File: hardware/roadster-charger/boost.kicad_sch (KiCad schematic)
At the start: 25 parts, among them Q1 CSD19532Q5B, U4 LTC3786EUD#TRPBF, U5 DAC70501MDQFR

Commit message: fix accidental schem. grid change, add footprints and MPNs
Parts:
- C12: footprint (none) -> Capacitor_SMD:C_0603_1608Metric; MPN (none) -> C0603C153K4REC7867
- C13: footprint (none) -> Capacitor_SMD:C_0603_1608Metric; MPN (none) -> C0603C221K1RAC7867
- C14: footprint (none) -> Capacitor_SMD:C_0805_2012Metric; MPN (none) -> CC0805KRX7R9BB104
- C15: footprint (none) -> Capacitor_SMD:C_0603_1608Metric; MPN (none) -> C1608X5R1E475K080AC
- C21, C22: footprint (none) -> Capacitor_SMD:C_0603_1608Metric; MPN (none) -> CL10B104KB8NNNC
- D5: MPN (none) -> BAS170WS-E3-08
- Q1: MPN (none) -> CSD19532Q5B
- R10: footprint (none) -> Resistor_SMD:R_0603_1608Metric; MPN (none) -> RC0603FR-07475KL
- R11: footprint (none) -> Resistor_SMD:R_0603_1608Metric; MPN (none) -> RC0603FR-1312K1L
- R12: footprint (none) -> Resistor_SMD:R_1206_3216Metric; MPN (none) -> WSLP12068L000FEA
- R13, R9: footprint (none) -> Resistor_SMD:R_0603_1608Metric; MPN (none) -> RC0603FR-078K66L
- U4: footprint QFN-16_UD -> LTC3786EUD_TRPBF:QFN-16_UD; Availability In Stock -> (none); Check_prices https://www.snapeda.com/parts/LTC3786EUD%23TRPBF/Analog+Dev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 -> (none); MANUFACTURER_PART_NUMBER ltc3786eud#pbf -> (none); MF Analog Devices -> (none); MP LTC3786EUD#TRPBF -> (none); MPN (none) -> LTC3786EUD#TRPBF; Purchase-URL https://pricing.snapeda.com/search?q=LTC3786EUD#TRPBF&ref=e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 -> (none); SnapEDA_Link https://www.snapeda.com/parts/LTC3786EUD%23TRPBF/Analog+Dev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 -> (none); VENDOR LinearTech -> (none)
- U5: footprint WSON8_2P1X2P1_TEX -> DAC70501:WSON8_2P1X2P1_TEX; MPN (none) -> DAC70501MDQFR
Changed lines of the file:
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@@
       (effects (font (size 1.524 1.524)))
     )
-    (property "Footprint" "WSON8_2P1X2P1_TEX" (at 134.62 107.95 0)
+    (property "Footprint" "DAC70501:WSON8_2P1X2P1_TEX" (at 134.62 107.95 0)
       (effects (font (size 1.27 1.27) italic) hide)
     )
     (property "Datasheet" "DAC70501MDQFR" (at 134.62 107.95 0)
       (effects (font (size 1.27 1.27) italic) hide)
+    )
+    (property "MPN" "DAC70501MDQFR" (at 134.62 111.76 0)
+      (effects (font (size 1.27 1.27)) hide)
     )
     (pin "1")
@@
       (effects (font (size 1.27 1.27)) (justify right))
     )
-    (property "Footprint" "" (at 191.77 146.05 0)
+    (property "Footprint" "Capacitor_SMD:C_0603_1608Metric" (at 191.77 146.05 0)
       (effects (font (size 1.27 1.27)) hide)
     )
     (property "Datasheet" "~" (at 191.77 146.05 0)
+      (effects (font (size 1.27 1.27)) hide)
+    )
+    (property "MPN" "C0603C221K1RAC7867" (at 191.77 146.05 0)
       (effects (font (size 1.27 1.27)) hide)
     )
@@
       (effects (font (size 1.27 1.27)) (justify left) hide)
     )
+    (property "MPN" "CSD19532Q5B" (at 259.08 133.35 0)
+      (effects (font (size 1.27 1.27)) hide)
+    )
     (pin "1")
     (pin "2")
@@
       (effects (font (size 1.27 1.27)) (justify right))
     )
-    (property "Footprint" "" (at 187.96 149.86 0)
+    (property "Footprint" "Capacitor_SMD:C_0603_1608Metric" (at 187.96 149.86 0)
       (effects (font (size 1.27 1.27)) hide)
     )
@@
       (effects (font (size 1.27 1.27)) hide)
     )
+    (property "MPN" "C0603C153K4REC7867" (at 187.96 149.86 0)
+      (effects (font (size 1.27 1.27)) hide)
+    )
     (pin "1")
     (pin "2")
@@
       (effects (font (size 1.27 1.27)) (justify right))
     )
-    (property "Footprint" "" (at 266.7 165.1 0)
+    (property "Footprint" "Resistor_SMD:R_0603_1608Metric" (at 266.7 165.1 0)
       (effects (font (size 1.27 1.27)) hide)
     )
     (property "Datasheet" "~" (at 266.7 165.1 0)
+      (effects (font (size 1.27 1.27)) hide)
+    )
+    (property "MPN" "RC0603FR-07475KL" (at 266.7 165.1 0)
       (effects (font (size 1.27 1.27)) hide)
     )
@@
       (effects (font (size 1.27 1.27)) hide)
     )
+    (property "MPN" "BAS170WS-E3-08" (at 241.3 151.13 0)
+      (effects (font (size 1.27 1.27)) hide)
+    )
     (pin "1")
     (pin "2")
@@
     (property "Datasheet" "http://www.ti.com/lit/gpn/csd19532q5b" (at 248.92 147.32 90)
       (effects (font (size 1.27 1.27)) (justify left) hide)
+    )
+    (property "MPN" "CSD19532Q5B" (at 248.92 147.32 0)
+      (effects (font (size 1.27 1.27)) hide)
     )
     (pin "1")
@@
       (effects (font (size 1.27 1.27)) (justify left))
     )
-    (property "Footprint" "" (at 172.72 111.76 0)
+    (property "Footprint" "Capacitor_SMD:C_0603_1608Metric" (at 172.72 111.76 0)
       (effects (font (size 1.27 1.27)) hide)
     )
     (property "Datasheet" "~" (at 172.72 111.76 0)
+      (effects (font (size 1.27 1.27)) hide)
+    )
+    (property "MPN" "CL10B104KB8NNNC" (at 172.72 111.76 0)
       (effects (font (size 1.27 1.27)) hide)
     )
@@
       (effects (font (size 1.27 1.27)))
     )
-    (property "Footprint" "QFN-16_UD" (at 176.53 110.49 0)
+    (property "Footprint" "LTC3786EUD_TRPBF:QFN-16_UD" (at 176.53 110.49 0)
       (effects (font (size 1.27 1.27)) (justify bottom) hide)
     )
     (property "Datasheet" "" (at 295.91 101.6 0)
       (effects (font (size 1.27 1.27)) hide)
-    )
-    (property "MF" "Analog Devices" (at 176.53 110.49 0)
-      (effects (font (size 1.27 1.27)) (justify bottom) hide)
-    )
-    (property "VENDOR" "LinearTech" (at 176.53 110.49 0)
-      (effects (font (size 1.27 1.27)) (justify bottom) hide)
     )
     (property "Description" "\nLow IQ Synchronous Boost Controller\n" (at 176.53 110.49 0)
@@
       (effects (font (size 1.27 1.27)) (justify bottom) hide)
     )
-    (property "Check_prices" "https://www.snapeda.com/parts/LTC3786EUD%23TRPBF/Analog+Devices/view-part/?ref=eda" (at 176.53 110.49 0)
-      (effects (font (size 1.27 1.27)) (justify bottom) hide)
-    )
-    (property "SnapEDA_Link" "https://www.snapeda.com/parts/LTC3786EUD%23TRPBF/Analog+Devices/view-part/?ref=snap" (at 176.53 110.49 0)
-      (effects (font (size 1.27 1.27)) (justify bottom) hide)
-    )
-    (property "MP" "LTC3786EUD#TRPBF" (at 176.53 110.49 0)
-      (effects (font (size 1.27 1.27)) (justify bottom) hide)
-    )
-    (property "Purchase-URL" "https://pricing.snapeda.com/search?q=LTC3786EUD#TRPBF&ref=eda" (at 176.53 110.49 0)
-      (effects (font (size 1.27 1.27)) (justify bottom) hide)
-    )
-    (property "Availability" "In Stock" (at 176.53 110.49 0)
-      (effects (font (size 1.27 1.27)) (justify bottom) hide)
-    )
-    (property "MANUFACTURER_PART_NUMBER" "ltc3786eud#pbf" (at 176.53 110.49 0)
-      (effects (font (size 1.27 1.27)) (justify bottom) hide)
+    (property "MPN" "LTC3786EUD#TRPBF" (at 176.53 110.49 0)
+      (effects (font (size 1.27 1.27)) hide)
     )
     (pin "1")
@@
       (effects (font (size 1.27 1.27)) (justify right))
     )
-    (property "Footprint" "" (at 191.77 120.65 0)
+    (property "Footprint" "Resistor_SMD:R_0603_1608Metric" (at 191.77 120.65 0)
       (effects (font (size 1.27 1.27)) hide)
     )
@@
       (effects (font (size 1.27 1.27)) hide)
     )
+    (property "MPN" "RC0603FR-078K66L" (at 191.77 120.65 0)
+      (effects (font (size 1.27 1.27)) hide)
+    )
     (pin "1")
     (pin "2")
@@
       (effects (font (size 1.27 1.27)) (justify left))
     )
-    (property "Footprint" "" (at 241.3 160.02 0)
+    (property "Footprint" "Capacitor_SMD:C_0603_1608Metric" (at 241.3 160.02 0)
       (effects (font (size 1.27 1.27)) hide)
     )
     (property "Datasheet" "~" (at 241.3 160.02 0)
+      (effects (font (size 1.27 1.27)) hide)
+    )
+    (property "MPN" "C1608X5R1E475K080AC" (at 241.3 160.02 0)
       (effects (font (size 1.27 1.27)) hide)
     )
@@
       (effects (font (size 1.27 1.27)) (justify left))
     )
-    (property "Footprint" "" (at 241.3 140.97 0)
+    (property "Footprint" "Capacitor_SMD:C_0805_2012Metric" (at 241.3 140.97 0)
       (effects (font (size 1.27 1.27)) hide)
     )
@@
       (effects (font (size 1.27 1.27)) hide)
     )
+    (property "MPN" "CC0805KRX7R9BB104" (at 241.3 140.97 0)
+      (effects (font (size 1.27 1.27)) hide)
+    )
     (pin "1")
     (pin "2")
@@
       (effects (font (size 1.27 1.27)) (justify right))
     )
-    (property "Footprint" "" (at 187.96 142.24 0)
+    (property "Footprint" "Resistor_SMD:R_0603_1608Metric" (at 187.96 142.24 0)
       (effects (font (size 1.27 1.27)) hide)
     )
@@
       (effects (font (size 1.27 1.27)) hide)
     )
+    (property "MPN" "RC0603FR-078K66L" (at 187.96 142.24 0)
+      (effects (font (size 1.27 1.27)) hide)
+    )
     (pin "1")
     (pin "2")
@@
       (effects (font (size 1.27 1.27)) (justify right))
     )
-    (property "Footprint" "" (at 266.7 172.72 0)
+    (property "Footprint" "Resistor_SMD:R_0603_1608Metric" (at 266.7 172.72 0)
       (effects (font (size 1.27 1.27)) hide)
     )
@@
       (effects (font (size 1.27 1.27)) hide)
     )
+    (property "MPN" "RC0603FR-1312K1L" (at 266.7 172.72 0)
+      (effects (font (size 1.27 1.27)) hide)
+    )
     (pin "1")
     (pin "2")
@@
       (effects (font (size 1.27 1.27)) (justify right))
     )
-    (property "Footprint" "" (at 119.38 106.68 0)
+    (property "Footprint" "Capacitor_SMD:C_0603_1608Metric" (at 119.38 106.68 0)
       (effects (font (size 1.27 1.27)) hide)
     )
     (property "Datasheet" "~" (at 119.38 106.68 0)
+      (effects (font (size 1.27 1.27)) hide)
+    )
+    (property "MPN" "CL10B104KB8NNNC" (at 119.38 106.68 0)
       (effects (font (size 1.27 1.27)) hide)
     )
@@
       (effects (font (size 1.27 1.27)) (justify left))
     )
-    (property "Footprint" "" (at 251.46 114.3 0)
+    (property "Footprint" "Resistor_SMD:R_1206_3216Metric" (at 251.46 114.3 0)
       (effects (font (size 1.27 1.27)) hide)
     )
     (property "Datasheet" "~" (at 251.46 114.3 0)
+      (effects (font (size 1.27 1.27)) hide)
+    )
+    (property "MPN" "WSLP12068L000FEA" (at 251.46 114.3 0)
       (effects (font (size 1.27 1.27)) hide)
     )
@@
     (pin "1")
     (pin "2")
-    (instances
-      (project "roadster-charger"
+    (pin "3")
+    (instances
+      (project "roadster-charger"

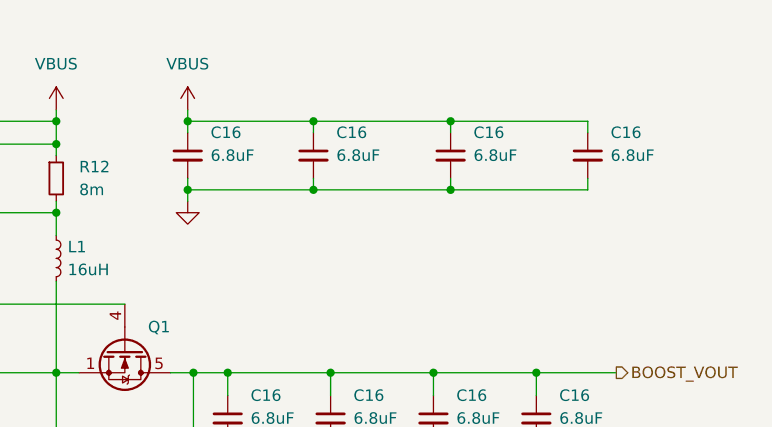
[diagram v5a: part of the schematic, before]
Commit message: edit ERC rules, clean up ERC errors, cleanup more off grid parts
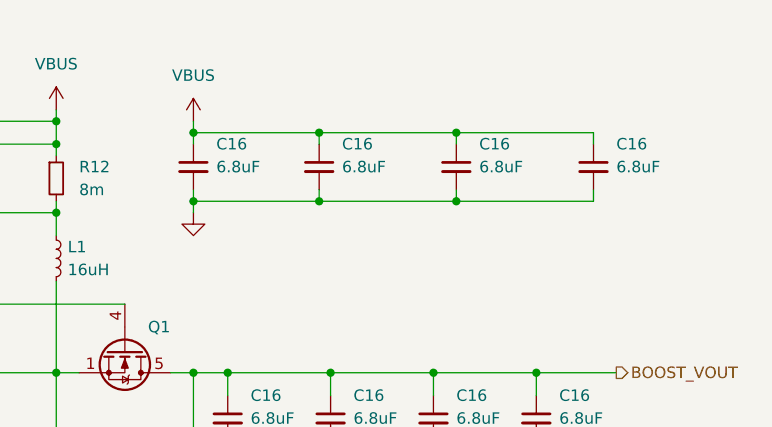
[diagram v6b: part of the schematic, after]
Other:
- moved on the sheet: C16

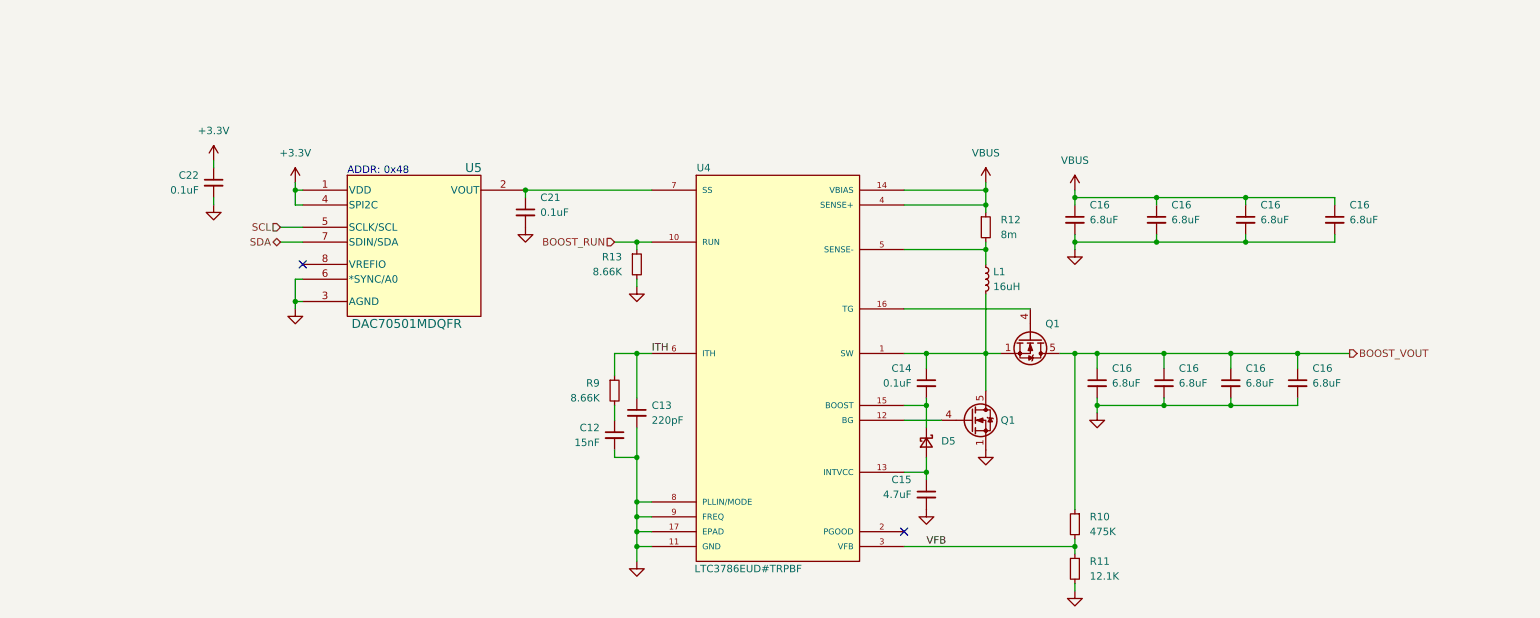
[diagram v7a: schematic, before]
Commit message: run schematic annotation to clean up error
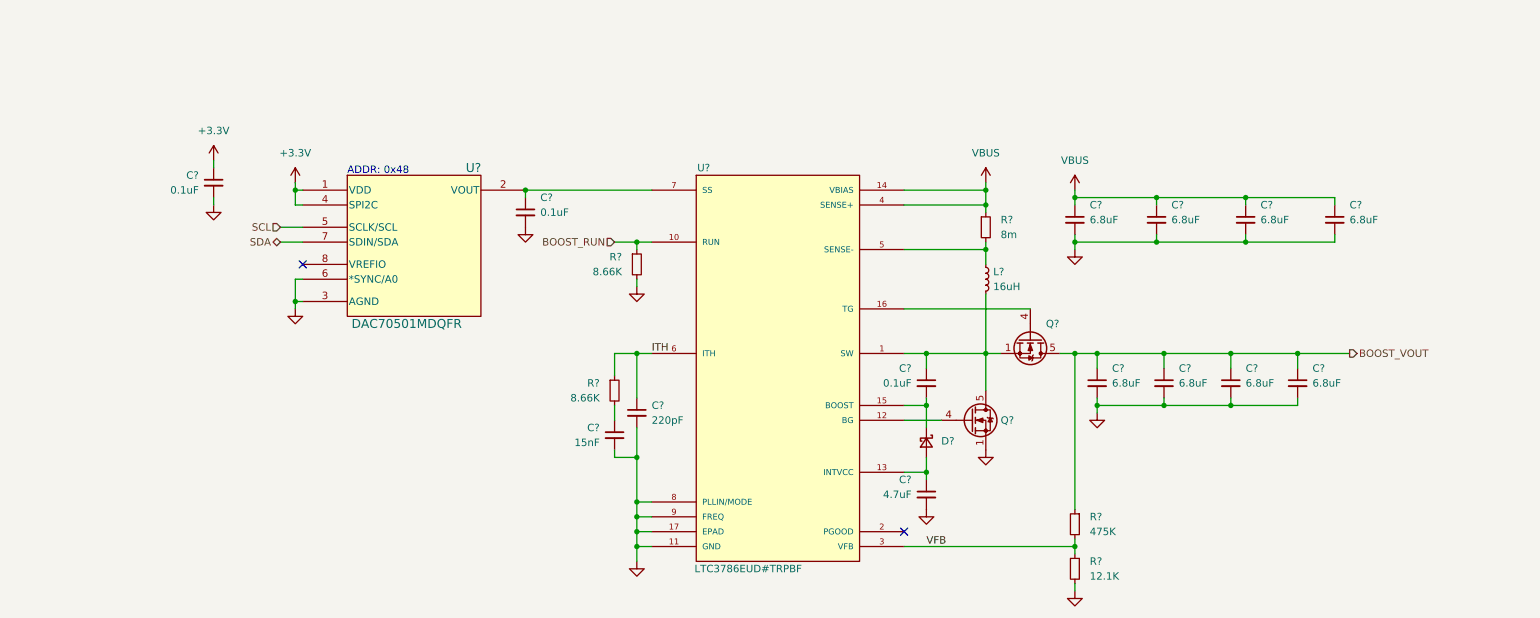
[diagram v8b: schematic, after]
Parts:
- renumbered C16 to C?, C13 to C?, C12 to C?, C21 to C?, C15 to C?, C14 to C?, C22 to C?, D5 to D?, L1 to L?, Q1 to Q?, R10 to R?, R13 to R?, R9 to R?, R11 to R?, R12 to R?, U5 to U?, U4 to U?
